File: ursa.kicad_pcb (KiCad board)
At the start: 2 copper layers, 241.2 x 99.3 mm, 99 parts, among them SW1 Kailh-Choc, SW10 Kailh-Choc, SW11 Kailh-Choc, SW12 Kailh-Choc, SW13 Kailh-Choc, SW14 Kailh-Choc, SW15 Kailh-Choc, SW16 Kailh-Choc, SW17 Kailh-Choc, SW18 Kailh-Choc, SW19 Kailh-Choc, SW2 Kailh-Choc, SW20 Kailh-Choc, SW21 Kailh-Choc, SW22 Kailh-Choc, SW23 Kailh-Choc, SW24 Kailh-Choc, SW25 Kailh-Choc, SW26 Kailh-Choc, SW27 Kailh-Choc, SW28 Kailh-Choc, SW29 Kailh-Choc, SW3 Kailh-Choc, SW30 Kailh-Choc, SW31 Kailh-Choc, SW32 Kailh-Choc, SW33 Kailh-Choc, SW34 Kailh-Choc, SW4 Kailh-Choc, SW5 Kailh-Choc, SW6 Kailh-Choc, SW7 Kailh-Choc, SW8 Kailh-Choc, SW9 Kailh-Choc, U1 nice_nano, U2 nice_nano

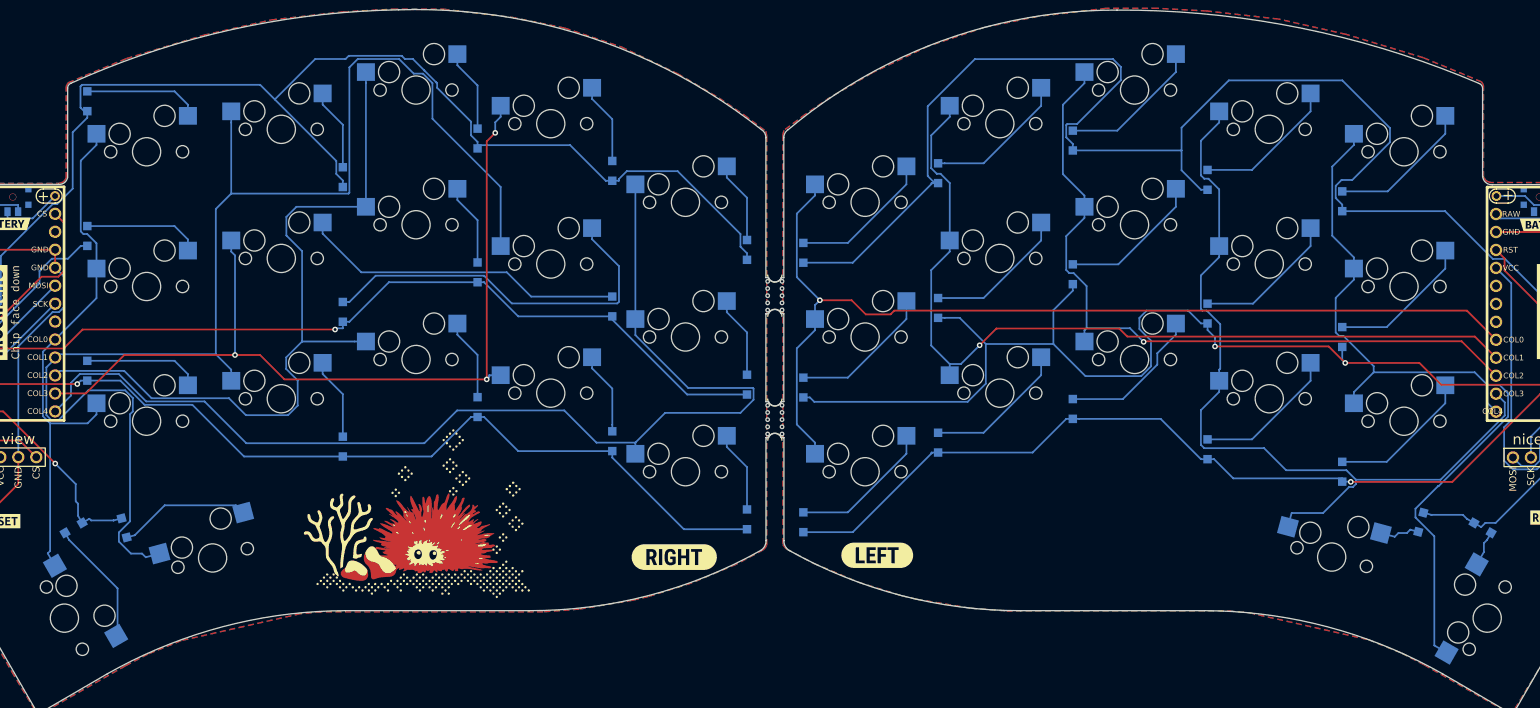
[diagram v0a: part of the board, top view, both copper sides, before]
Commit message: mouser bite added as library
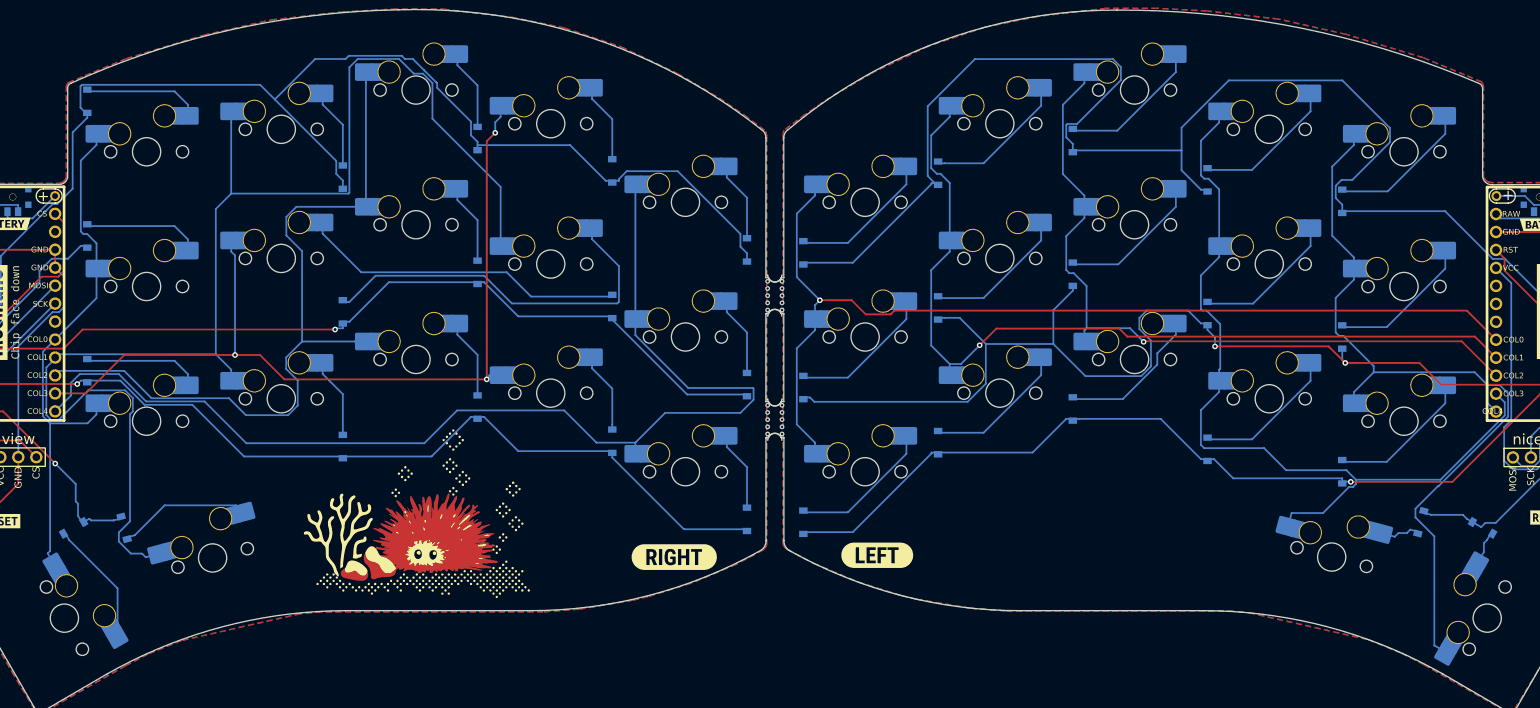
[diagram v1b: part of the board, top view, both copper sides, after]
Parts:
- removed 1-mouse-bite-2mm-slot, 2-mouse-bite-2mm-slot: VAL**, Duckyb-Parts:mouse-bite-5mm-slot-with-space-for-track
- added H1: Mouser Bite, extra:mouse-bite-2mm-slot-with-space-for-track, F.Cu at (147.6, 86.2)
- added H2: MouserBite, extra:mouse-bite-2mm-slot-with-space-for-track, F.Cu at (147.6, 103.8)
- D1, D10, D11, D12, D13, D14, D15, D16, D17, D18, D19, D2, D20, D21, D22, D23, D24, D25, D26, D27, D28, D29, D3, D30, D31, D32, D33, D34, D4, D5, D6, D7, D8, D9: footprint Diode_SMD:Nexperia_CFP3_SOD-123W -> Diode_SMD:D_SOD-123
- SW1, SW10, SW11, SW12, SW13, SW14, SW15, SW16, SW17, SW18, SW19, SW2, SW20, SW21, SW22, SW23, SW24, SW25, SW26, SW27, SW28, SW29, SW3, SW30, SW31, SW32, SW33, SW34, SW4, SW5, SW6, SW7, SW8, SW9: footprint MX_Only:MXOnly-1U-Hotswap -> marbastlib-mx:SW_MX_HS_1u; moved to B.Cu
- turned SW1 to 180 degrees
- turned SW10 to 180 degrees
- turned SW11 to 180 degrees
- turned SW12 to 180 degrees
- turned SW13 to 180 degrees
- turned SW14 to 180 degrees
- turned SW15 to 180 degrees
- turned SW16 to 165 degrees
- turned SW17 to -120 degrees
- turned SW18 to 180 degrees
- turned SW19 to 180 degrees
- turned SW2 to 180 degrees
- turned SW20 to 180 degrees
- turned SW21 to 180 degrees
- turned SW22 to 180 degrees
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
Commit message: library changes with new routes
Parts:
- SW_POWER0, SW_POWER1: footprint * duckyb-collection:SPDT_C128955 -> marbastlib-various:SW_MSK12C02-HB
- moved D28 22.0 mm to (67.1, 111.1)
- moved D18 22.0 mm to (67.1, 73.0)
- moved D23 22.0 mm to (67.1, 92.1)
- moved SW24 0.79 mm to (115.9, 81.0)
- moved SW26 0.79 mm to (77.8, 81.8)
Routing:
- net ROW0: track 204.8 -> 141.4 mm
- net ROW1: track 158.6 -> 202.0 mm, vias 2 -> 0
- net R_COL1: track 189.2 -> 154.5 mm
- net R_ROW1: track 154.3 -> 136.5 mm
- net R_COL4: track 156.7 -> 139.1 mm
- net R_NVCS: track 54.5 -> 37.4 mm
- net R_COL0: track 75.9 -> 90.6 mm
- net R_ROW2: track 127.7 -> 141.8 mm, vias 1 -> 0
- net Net-(D24-Pad2): track 54.3 -> 40.5 mm
- net Net-(D26-Pad2): track 46.2 -> 57.1 mm
- net R_COL2: track 106.9 -> 98.0 mm
- net Net-(D16-Pad2): track 5.81 -> 14.7 mm
- net COL4: track 114.2 -> 106.9 mm
- net RESET: track 50.8 -> 43.5 mm
- net COL2: track 104.1 -> 111.1 mm, vias 1 -> 0
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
